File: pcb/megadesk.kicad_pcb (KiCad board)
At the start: 2 copper layers, 42.2 x 32.8 mm, 25 parts, among them J1 Interface, J2 FFC, J3 AVR-ISP-6, U1 L7812, U2 L7805, U3 ATtiny841-SS, U4 MCP2003B

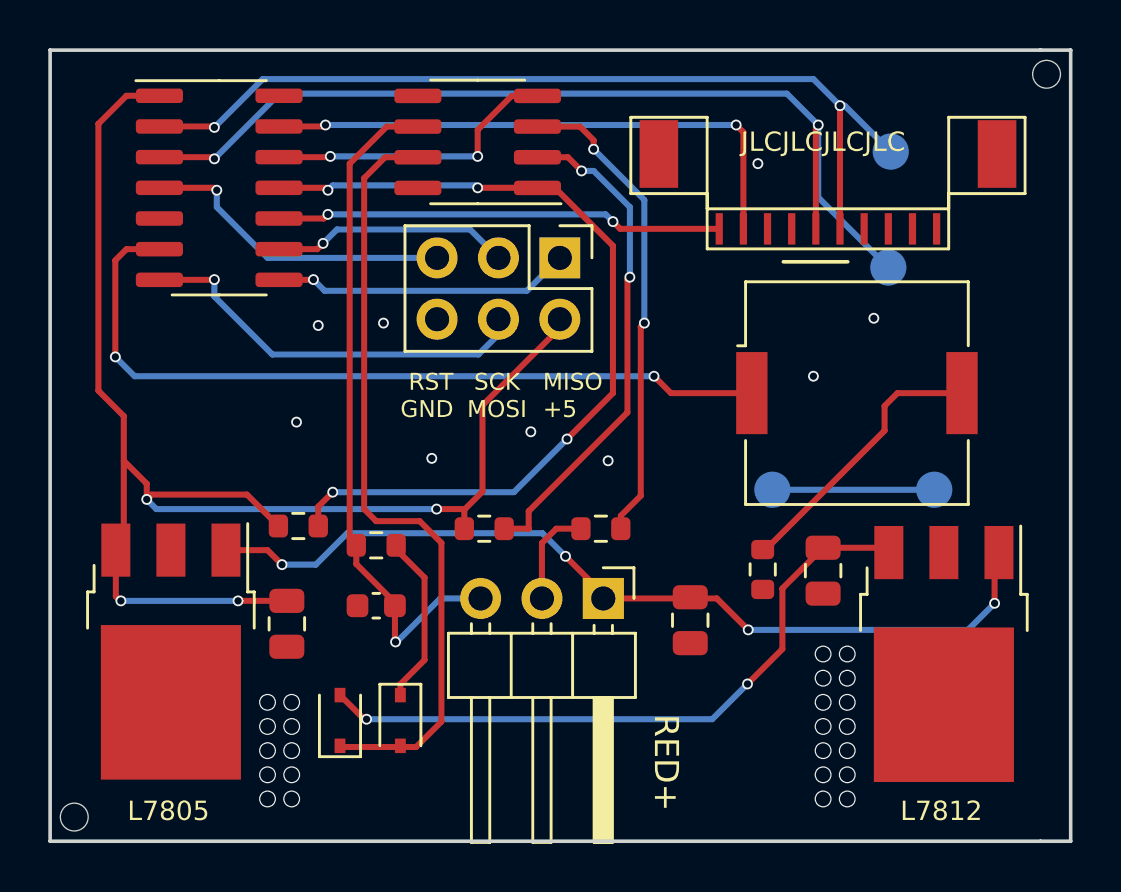
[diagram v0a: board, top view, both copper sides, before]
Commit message: revise LDO's
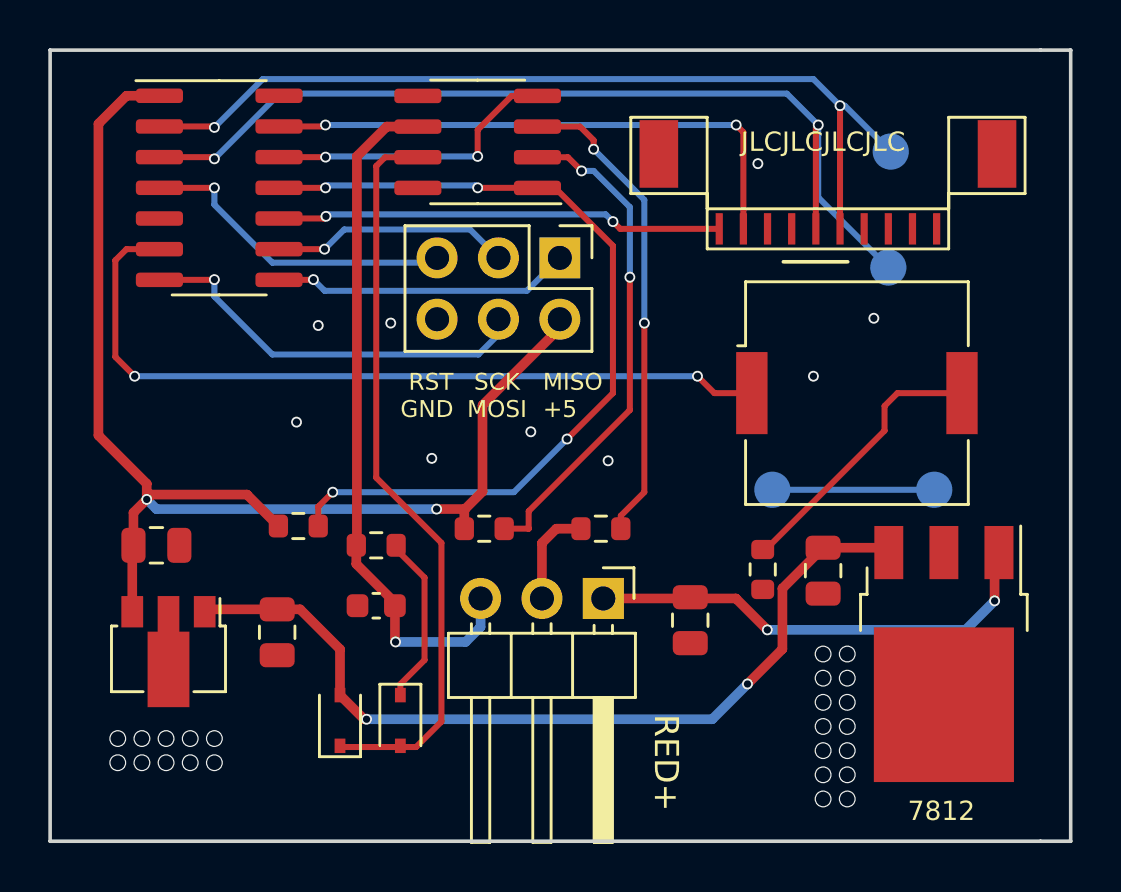
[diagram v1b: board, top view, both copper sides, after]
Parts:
- removed REF** (x2): MountingHole_2.1mm, MountingHole:MountingHole_2.1mm
- added C2: 0.33uF, Capacitor_SMD:C_0805_2012Metric, F.Cu at (108.1, 128.7)
- U1: value L7812 -> 7812
- U2: value L7805 -> 7805; footprint Package_TO_SOT_SMD:TO-252-3_TabPin2 -> Package_TO_SOT_SMD:SOT-89-3
- moved C5 6.30 mm to (103.1, 125.1), turned to 0 degrees
- moved U2 0.32 mm to (103.6, 129.8)
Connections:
- U2 pad 1: +24V -> +12V
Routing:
- net +24V: track 37.0 -> 19.3 mm, vias 4 -> 2
- net +12V: track 27.6 -> 35.9 mm
- net +5V: track 62.1 -> 54.0 mm, vias 4 -> 2
- net Net-(D1-Pad1): track 32.1 -> 30.7 mm
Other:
- board text added: "megadesk v9"
- board text removed: "megadesk v8"

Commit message: simplify caps
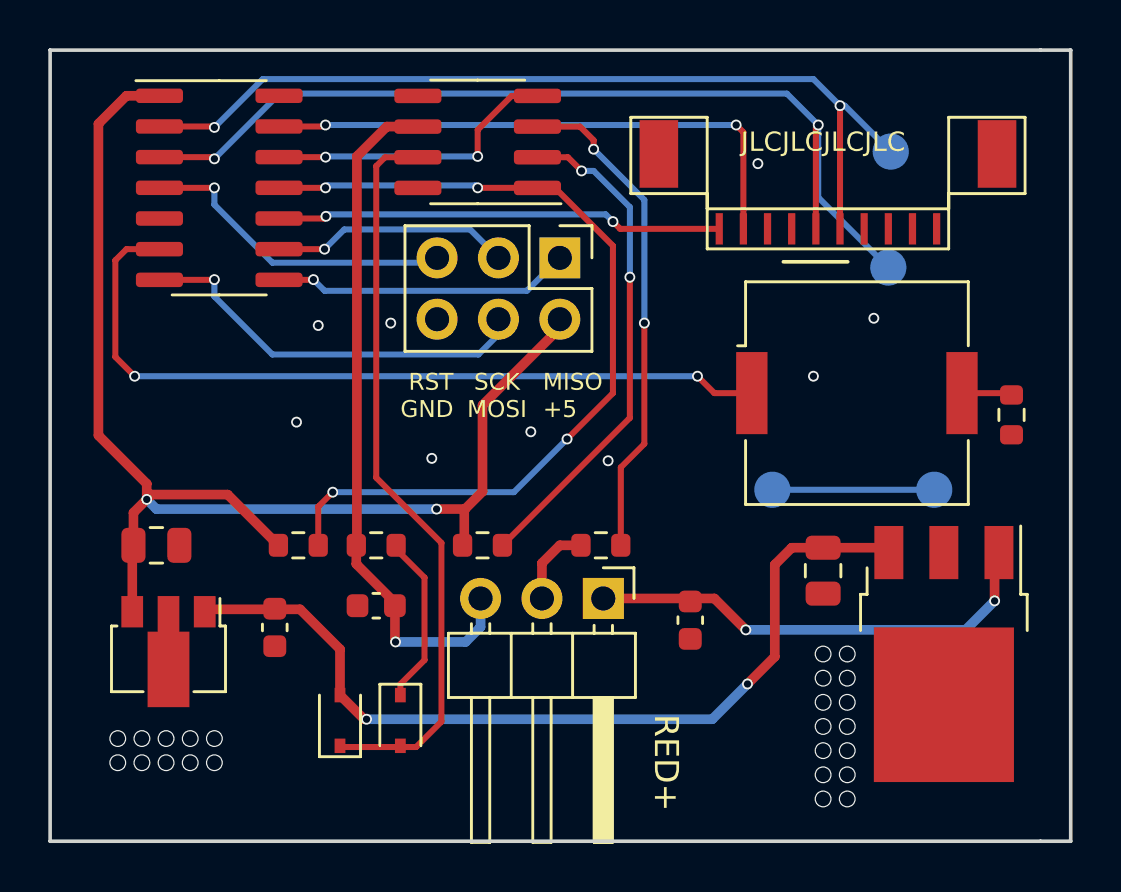
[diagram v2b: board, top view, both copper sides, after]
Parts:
- C1, C2: value 0.33uF -> 220pF; footprint Capacitor_SMD:C_0805_2012Metric -> Capacitor_SMD:C_0603_1608Metric
- moved R1 12.1 mm to (138.5, 119.7)
- moved R3 0.80 mm to (109.0, 125.1)
- moved R4 0.69 mm to (116.6, 125.1)
- moved R5 0.69 mm to (121.5, 125.1)
- moved C2 0.22 mm to (108.0, 128.5)
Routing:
- net Net-(BZ1-Pad2): track 12.0 -> 2.08 mm
- net +5V: track 54.0 -> 55.1 mm
- net Net-(R3-Pad2): track 35.9 -> 36.7 mm
- net GND: track 4.15 -> 3.38 mm
- net +12V: track 35.9 -> 36.6 mm
- net Net-(R5-Pad1): track 19.9 -> 20.6 mm

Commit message: ugh. fix bad pins.
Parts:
- U2: value 7805 -> HT7550-1
- moved C2 2.00 mm to (108.1, 130.5)
- moved R4 0.40 mm to (116.6, 124.7)
- moved R5 0.40 mm to (121.5, 124.7)
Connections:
- U2 pad 1: +12V -> GND
- U2 pad 2: GND -> +12V
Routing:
- net GND: track 3.38 -> 6.73 mm, vias 33 -> 27
- net +12V: track 36.6 -> 37.8 mm, vias 2 -> 12
- added copper zone on B.Cu, net +12V
- added copper zone on F.Cu, net +12V

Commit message: kicad v7
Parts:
- moved R4 1.97 mm to (118.4, 123.9)
- moved R5 0.94 mm to (122.0, 123.9)
- moved J1 0.50 mm to (121.6, 126.8)
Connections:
- BZ1 pad 1: Net-(BZ1-Pad1) -> (no net)
- BZ1 pad 2: Net-(BZ1-Pad2) -> (no net)
- D1 pad 1: Net-(D1-Pad1) -> (no net)
- D2 pad 1: Net-(D2-Pad1) -> (no net)
- D2 pad 2: Net-(D1-Pad1) -> Net-(D1-K)
- J2 pad 1: unconnected-(J2-Pad1) -> (no net)
- J2 pad 2: unconnected-(J2-Pad2) -> (no net)
- J2 pad 3: unconnected-(J2-Pad3) -> (no net)
- J2 pad 4: unconnected-(J2-Pad4) -> (no net)
- J2 pad 8: unconnected-(J2-Pad8) -> (no net)
- R1 pad 1: Net-(BZ1-Pad2) -> Net-(BZ1-+)
- R3 pad 2: Net-(R3-Pad2) -> (no net)
- R4 pad 1: Net-(R4-Pad1) -> (no net)
- R5 pad 1: Net-(R5-Pad1) -> (no net)
- R6 pad 1: Net-(D2-Pad1) -> Net-(D2-K)
- U3 pad 11: Net-(R3-Pad2) -> Net-(U3-PA2)
- U3 pad 12: Net-(U3-Pad12) -> (no net)
- U3 pad 5: unconnected-(U3-Pad5) -> (no net)
- U3 pad 6: Net-(BZ1-Pad1) -> Net-(BZ1--)
- U4 pad 1: Net-(R3-Pad2) -> Net-(U3-PA2)
- U4 pad 2: Net-(R4-Pad1) -> Net-(U4-CS)
- U4 pad 3: Net-(R5-Pad1) -> Net-(U4-WAKE)
- U4 pad 4: Net-(U3-Pad12) -> Net-(U3-PA1)
- U4 pad 7: Net-(D1-Pad1) -> Net-(D1-K)
- U4 pad 8: unconnected-(U4-Pad8) -> (no net)
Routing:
- net Net-(U3-PA2): track 0.00 -> 36.7 mm, vias 0 -> 4
- net Net-(R3-Pad2): track 36.7 -> 0.00 mm, vias 4 -> 0
- net Net-(BZ1-Pad1): track 32.5 -> 0.00 mm, vias 2 -> 0
- net Net-(BZ1--): track 0.00 -> 32.5 mm, vias 0 -> 2
- net Net-(D1-Pad1): track 30.7 -> 0.00 mm
- net Net-(D1-K): track 0.00 -> 30.7 mm
- net Net-(R4-Pad1): track 20.7 -> 0.00 mm, vias 2 -> 0
- net Net-(R5-Pad1): track 20.2 -> 0.00 mm, vias 2 -> 0
- net Net-(U4-WAKE): track 0.00 -> 19.2 mm, vias 0 -> 2
- net Net-(U4-CS): track 0.00 -> 18.9 mm, vias 0 -> 2
- net Net-(U3-Pad12): track 12.4 -> 0.00 mm, vias 2 -> 0
- net Net-(U3-PA1): track 0.00 -> 12.4 mm, vias 0 -> 2
- net Net-(D2-Pad1): track 6.90 -> 0.00 mm
- net Net-(D2-K): track 0.00 -> 6.90 mm
- net Net-(BZ1-Pad2): track 2.08 -> 0.00 mm
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
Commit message: fix silkscreen kibot and v7
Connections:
- BZ1 pad 1: (no net) -> Net-(BZ1--)
- BZ1 pad 2: (no net) -> Net-(BZ1-+)
- D1 pad 1: (no net) -> Net-(D1-K)
- D2 pad 1: (no net) -> Net-(D2-K)
- J2 pad 1: (no net) -> unconnected-(J2-Pin_1-Pad1)
- J2 pad 2: (no net) -> unconnected-(J2-Pin_2-Pad2)
- J2 pad 3: (no net) -> unconnected-(J2-Pin_3-Pad3)
- J2 pad 4: (no net) -> unconnected-(J2-Pin_4-Pad4)
- J2 pad 8: (no net) -> unconnected-(J2-Pin_8-Pad8)
- R3 pad 2: (no net) -> Net-(U3-PA2)
- R4 pad 1: (no net) -> Net-(U4-CS)
- R5 pad 1: (no net) -> Net-(U4-WAKE)
- U3 pad 12: (no net) -> Net-(U3-PA1)
- U3 pad 5: (no net) -> unconnected-(U3-PB2-Pad5)
- U4 pad 8: (no net) -> unconnected-(U4-VREN-Pad8)
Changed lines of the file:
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@@
   (net 21 "Net-(U3-PA1)")
   (net 22 "Net-(TP1-Pad1)")
+  (net 23 "unconnected-(J2-Pin_1-Pad1)")
+  (net 24 "unconnected-(J2-Pin_2-Pad2)")
+  (net 25 "unconnected-(J2-Pin_3-Pad3)")
+  (net 26 "unconnected-(J2-Pin_4-Pad4)")
+  (net 27 "unconnected-(J2-Pin_8-Pad8)")
+  (net 28 "unconnected-(U3-PB2-Pad5)")
+  (net 29 "unconnected-(U4-VREN-Pad8)")
   (footprint "Connector_PinHeader_2.54mm:PinHeader_1x03_P2.54mm_Horizontal" (layer "F.Cu")
     (at 121.6 126.8 -90)
@@
       (stroke (width 0.1) (type solid)) (layer "F.Fab"))
     (pad "1" smd rect (at -1.05 0 90) (size 0.6 0.45) (layers "F.Cu" "F.Paste" "F.Mask")
-      (pinfunction "K") (pintype "passive"))
+      (net 12 "Net-(D1-K)") (pinfunction "K") (pintype "passive"))
     (pad "2" smd rect (at 1.05 0 90) (size 0.6 0.45) (layers "F.Cu" "F.Paste" "F.Mask")
       (net 3 "+12V") (pinfunction "A") (pintype "passive"))
@@
     (pad "" smd rect locked (at 7 3.1 180) (size 1.6 2.8) (layers "F.Cu" "F.Paste" "F.Mask"))
     (pad "1" smd rect locked (at -4.5 0 180) (size 0.3 1.3) (layers "F.Cu" "F.Paste" "F.Mask")
-      (pinfunction "Pin_1") (pintype "passive+no_connect"))
+      (net 23 "unconnected-(J2-Pin_1-Pad1)") (pinfunction "Pin_1") (pintype "passive+no_connect"))
     (pad "2" smd rect locked (at -3.5 0 180) (size 0.3 1.3) (layers "F.Cu" "F.Paste" "F.Mask")
-      (pinfunction "Pin_2") (pintype "passive+no_connect"))
+      (net 24 "unconnected-(J2-Pin_2-Pad2)") (pinfunction "Pin_2") (pintype "passive+no_connect"))
     (pad "3" smd rect locked (at -2.5 0 180) (size 0.3 1.3) (layers "F.Cu" "F.Paste" "F.Mask")
-      (pinfunction "Pin_3") (pintype "passive+no_connect"))
+      (net 25 "unconnected-(J2-Pin_3-Pad3)") (pinfunction "Pin_3") (pintype "passive+no_connect"))
     (pad "4" smd rect locked (at -1.5 0 180) (size 0.3 1.3) (layers "F.Cu" "F.Paste" "F.Mask")
-      (pinfunction "Pin_4") (pintype "passive+no_connect"))
+      (net 26 "unconnected-(J2-Pin_4-Pad4)") (pinfunction "Pin_4") (pintype "passive+no_connect"))
     (pad "5" smd rect locked (at -0.5 0 180) (size 0.3 1.3) (layers "F.Cu" "F.Paste" "F.Mask")
       (net 14 "Bup") (pinfunction "Pin_5") (pintype "passive"))
@@
       (net 2 "GND") (pinfunction "Pin_7") (pintype "passive"))
     (pad "8" smd rect locked (at 2.5 0 180) (size 0.3 1.3) (layers "F.Cu" "F.Paste" "F.Mask")
-      (pinfunction "Pin_8") (pintype "passive+no_connect"))
+      (net 27 "unconnected-(J2-Pin_8-Pad8)") (pinfunction "Pin_8") (pintype "passive+no_connect"))
     (pad "9" smd rect locked (at 3.5 0 180) (size 0.3 1.3) (layers "F.Cu" "F.Paste" "F.Mask")
       (net 16 "B9") (pinfunction "Pin_9") (pintype "passive"))
@@
       (stroke (width 0.1) (type solid)) (layer "F.Fab"))
     (pad "1" smd roundrect (at -0.825 0 180) (size 0.8 0.95) (layers "F.Cu" "F.Paste" "F.Mask") (roundrect_rratio 0.25)
-      (pintype "passive"))
+      (net 19 "Net-(U4-CS)") (pintype "passive"))
     (pad "2" smd roundrect (at 0.825 0 180) (size 0.8 0.95) (layers "F.Cu" "F.Paste" "F.Mask") (roundrect_rratio 0.25)
       (net 1 "+5V") (pintype "passive"))
@@
       (stroke (width 0.1) (type solid)) (layer "F.Fab"))
     (pad "1" smd rect (at -4.35 0) (size 1.3 3.4) (layers "F.Cu" "F.Paste" "F.Mask")
-      (pinfunction "-") (pintype "passive"))
+      (net 10 "Net-(BZ1--)") (pinfunction "-") (pintype "passive"))
     (pad "2" smd rect (at 4.35 0) (size 1.3 3.4) (layers "F.Cu" "F.Paste" "F.Mask")
-      (pinfunction "+") (pintype "passive"))
+      (net 11 "Net-(BZ1-+)") (pinfunction "+") (pintype "passive"))
     (model "${KICAD6_3DMODEL_DIR}/Buzzer_Beeper.3dshapes/Buzzer_Murata_PKMCS0909E.wrl"
       (offset (xyz 0 0 0))
@@
       (stroke (width 0.1) (type solid)) (layer "F.Fab"))
     (pad "1" smd rect (at -1.05 0 270) (size 0.6 0.45) (layers "F.Cu" "F.Paste" "F.Mask")
-      (pinfunction "K") (pintype "passive"))
+      (net 13 "Net-(D2-K)") (pinfunction "K") (pintype "passive"))
     (pad "2" smd rect (at 1.05 0 270) (size 0.6 0.45) (layers "F.Cu" "F.Paste" "F.Mask")
       (net 12 "Net-(D1-K)") (pinfunction "A") (pintype "passive"))
@@
       (net 8 "RST") (pinfunction "~{RESET}/PB3") (pintype "bidirectional"))
     (pad "5" smd roundrect (at -2.475 1.27) (size 1.95 0.6) (layers "F.Cu" "F.Paste" "F.Mask") (roundrect_rratio 0.25)
-      (pinfunction "PB2") (pintype "bidirectional+no_connect"))
+      (net 28 "unconnected-(U3-PB2-Pad5)") (pinfunction "PB2") (pintype "bidirectional+no_connect"))
     (pad "6" smd roundrect (at -2.475 2.54) (size 1.95 0.6) (layers "F.Cu" "F.Paste" "F.Mask") (roundrect_rratio 0.25)
       (net 10 "Net-(BZ1--)") (pinfunction "PA7") (pintype "bidirectional"))
@@
       (net 18 "Net-(U3-PA2)") (pinfunction "PA2") (pintype "bidirectional"))
     (pad "12" smd roundrect (at 2.475 -1.27) (size 1.95 0.6) (layers "F.Cu" "F.Paste" "F.Mask") (roundrect_rratio 0.25)
-      (pinfunction "PA1") (pintype "bidirectional"))
+      (net 21 "Net-(U3-PA1)") (pinfunction "PA1") (pintype "bidirectional"))
     (pad "13" smd roundrect (at 2.475 -2.54) (size 1.95 0.6) (layers "F.Cu" "F.Paste" "F.Mask") (roundrect_rratio 0.25)
       (net 16 "B9") (pinfunction "AREF/PA0") (pintype "bidirectional"))
@@
       (net 1 "+5V") (pintype "passive"))
     (pad "2" smd roundrect (at 0.825 0) (size 0.8 0.95) (layers "F.Cu" "F.Paste" "F.Mask") (roundrect_rratio 0.25)
-      (pintype "passive"))
+      (net 18 "Net-(U3-PA2)") (pintype "passive"))
     (model "${KISYS3DMOD}/Resistor_SMD.3dshapes/R_0603_1608Metric.wrl"
       (offset (xyz 0 0 0))
@@
       (stroke (width 0.1) (type solid)) (layer "F.Fab"))
     (pad "1" smd roundrect (at -0.825 0 180) (size 0.8 0.95) (layers "F.Cu" "F.Paste" "F.Mask") (roundrect_rratio 0.25)
-      (pintype "passive"))
+      (net 20 "Net-(U4-WAKE)") (pintype "passive"))
     (pad "2" smd roundrect (at 0.825 0 180) (size 0.8 0.95) (layers "F.Cu" "F.Paste" "F.Mask") (roundrect_rratio 0.25)
       (net 2 "GND") (pintype "passive"))
@@
       (net 12 "Net-(D1-K)") (pinfunction "VBB") (pintype "power_in"))
     (pad "8" smd roundrect (at 2.475 -1.905 180) (size 1.95 0.6) (layers "F.Cu" "F.Paste" "F.Mask") (roundrect_rratio 0.25)
-      (pinfunction "VREN") (pintype "output+no_connect"))
+      (net 29 "unconnected-(U4-VREN-Pad8)") (pinfunction "VREN") (pintype "output+no_connect"))
     (model "${KICAD6_3DMODEL_DIR}/Package_SO.3dshapes/SOIC-8_3.9x4.9mm_P1.27mm.wrl"
       (offset (xyz 0 0 0))

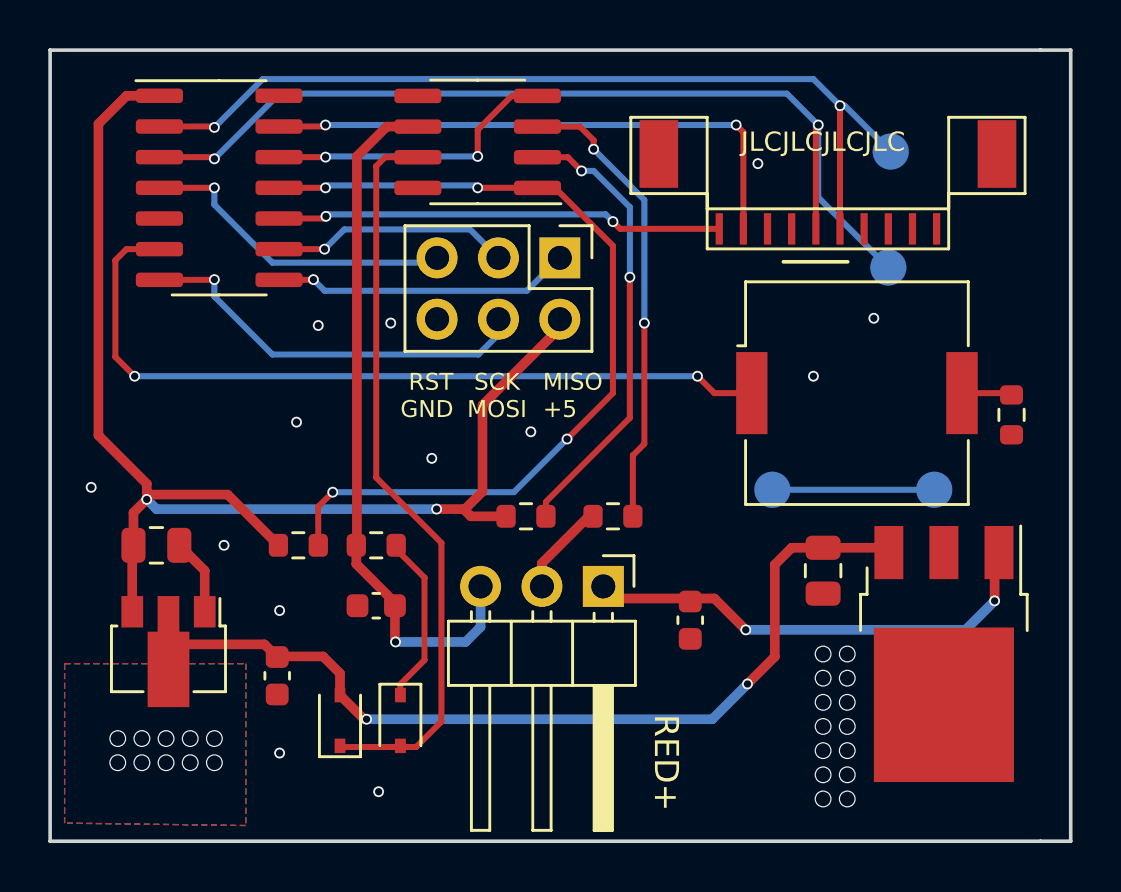
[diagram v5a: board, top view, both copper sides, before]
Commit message: change board by 0.5mm
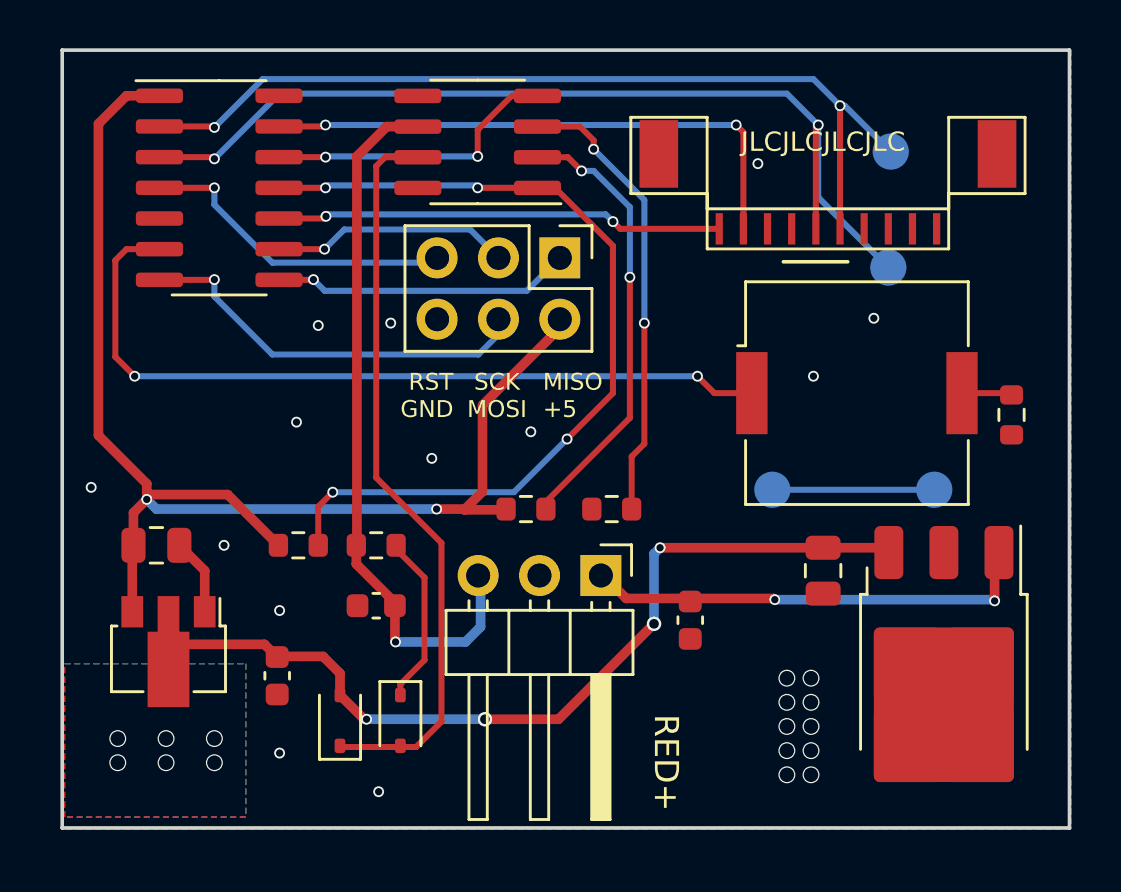
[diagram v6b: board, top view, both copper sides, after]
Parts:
- moved U1 0.84 mm to (135.7, 130.4)
- moved J1 0.46 mm to (121.5, 126.3)
- moved R5 0.30 mm to (122.0, 123.6)
- moved R4 0.30 mm to (118.4, 123.6)
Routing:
- net GND: track 7.06 -> 3.18 mm, vias 27 -> 23
- net +12V: track 37.8 -> 36.3 mm, vias 12 -> 10
- net +24V: track 19.5 -> 18.5 mm
- net MOSI: track 16.7 -> 16.1 mm
- net Net-(U4-CS): track 18.9 -> 18.3 mm
- net +5V: track 55.4 -> 54.9 mm
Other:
- board size 42.2 x 32.8 mm -> 41.7 x 32.2 mm
- board text added: "megadesk v10"
- board text removed: "megadesk v9"
